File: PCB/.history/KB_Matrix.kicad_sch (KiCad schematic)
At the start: 42 parts

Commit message: Started trying to route the traces
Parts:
- S1, S10, S11, S12, S13, S14, S15, S16, S17, S18, S19, S2, S20, S21, S3, S4, S5, S6, S7, S8, S9: footprint (none) -> Keyboard switches:Kailh_socket_PG1350
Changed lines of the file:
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@@
 			)
 		)
-		(property "Footprint" ""
+		(property "Footprint" "Keyboard switches:Kailh_socket_PG1350"
 			(at 116.84 92.71 0)
 			(hide yes)
@@
 			)
 		)
-		(property "Footprint" ""
+		(property "Footprint" "Keyboard switches:Kailh_socket_PG1350"
 			(at 137.16 106.68 0)
 			(hide yes)
@@
 			)
 		)
-		(property "Footprint" ""
+		(property "Footprint" "Keyboard switches:Kailh_socket_PG1350"
 			(at 137.16 92.71 0)
 			(hide yes)
@@
 			)
 		)
-		(property "Footprint" ""
+		(property "Footprint" "Keyboard switches:Kailh_socket_PG1350"
 			(at 137.16 64.77 0)
 			(hide yes)
@@
 			)
 		)
-		(property "Footprint" ""
+		(property "Footprint" "Keyboard switches:Kailh_socket_PG1350"
 			(at 116.84 64.77 0)
 			(hide yes)
@@
 			)
 		)
-		(property "Footprint" ""
+		(property "Footprint" "Keyboard switches:Kailh_socket_PG1350"
 			(at 147.32 78.74 0)
 			(hide yes)
@@
 			)
 		)
-		(property "Footprint" ""
+		(property "Footprint" "Keyboard switches:Kailh_socket_PG1350"
 			(at 127 92.71 0)
 			(hide yes)
@@
 			)
 		)
-		(property "Footprint" ""
+		(property "Footprint" "Keyboard switches:Kailh_socket_PG1350"
 			(at 106.68 92.71 0)
 			(hide yes)
@@
 			)
 		)
-		(property "Footprint" ""
+		(property "Footprint" "Keyboard switches:Kailh_socket_PG1350"
 			(at 127 120.65 0)
 			(hide yes)
@@
 			)
 		)
-		(property "Footprint" ""
+		(property "Footprint" "Keyboard switches:Kailh_socket_PG1350"
 			(at 116.84 78.74 0)
 			(hide yes)
@@
 			)
 		)
-		(property "Footprint" ""
+		(property "Footprint" "Keyboard switches:Kailh_socket_PG1350"
 			(at 127 64.77 0)
 			(hide yes)
@@
 			)
 		)
-		(property "Footprint" ""
+		(property "Footprint" "Keyboard switches:Kailh_socket_PG1350"
 			(at 106.68 64.77 0)
 			(hide yes)
@@
 			)
 		)
-		(property "Footprint" ""
+		(property "Footprint" "Keyboard switches:Kailh_socket_PG1350"
 			(at 106.68 120.65 0)
 			(hide yes)
@@
 			)
 		)
-		(property "Footprint" ""
+		(property "Footprint" "Keyboard switches:Kailh_socket_PG1350"
 			(at 106.68 78.74 0)
 			(hide yes)
@@
 			)
 		)
-		(property "Footprint" ""
+		(property "Footprint" "Keyboard switches:Kailh_socket_PG1350"
 			(at 106.68 106.68 0)
 			(hide yes)
@@
 			)
 		)
-		(property "Footprint" ""
+		(property "Footprint" "Keyboard switches:Kailh_socket_PG1350"
 			(at 116.84 106.68 0)
 			(hide yes)
@@
 			)
 		)
-		(property "Footprint" ""
+		(property "Footprint" "Keyboard switches:Kailh_socket_PG1350"
 			(at 137.16 78.74 0)
 			(hide yes)
@@
 			)
 		)
-		(property "Footprint" ""
+		(property "Footprint" "Keyboard switches:Kailh_socket_PG1350"
 			(at 147.32 64.77 0)
 			(hide yes)
@@
 			)
 		)
-		(property "Footprint" ""
+		(property "Footprint" "Keyboard switches:Kailh_socket_PG1350"
 			(at 116.84 120.65 0)
 			(hide yes)
@@
 			)
 		)
-		(property "Footprint" ""
+		(property "Footprint" "Keyboard switches:Kailh_socket_PG1350"
 			(at 127 106.68 0)
 			(hide yes)
@@
 			)
 		)
-		(property "Footprint" ""
+		(property "Footprint" "Keyboard switches:Kailh_socket_PG1350"
 			(at 127 78.74 0)
 			(hide yes)

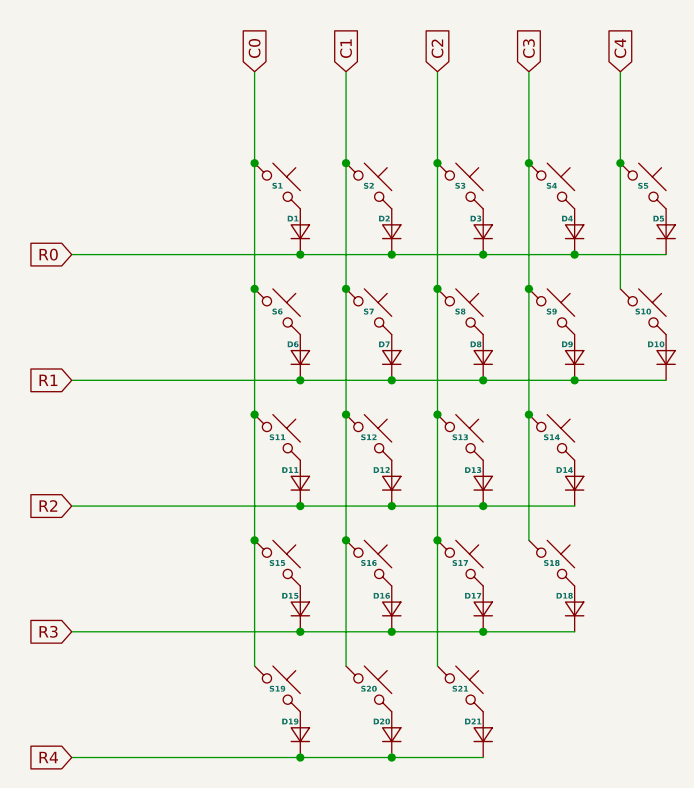
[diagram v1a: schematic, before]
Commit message: Done with the kiCad Matrix layout placement in sketch
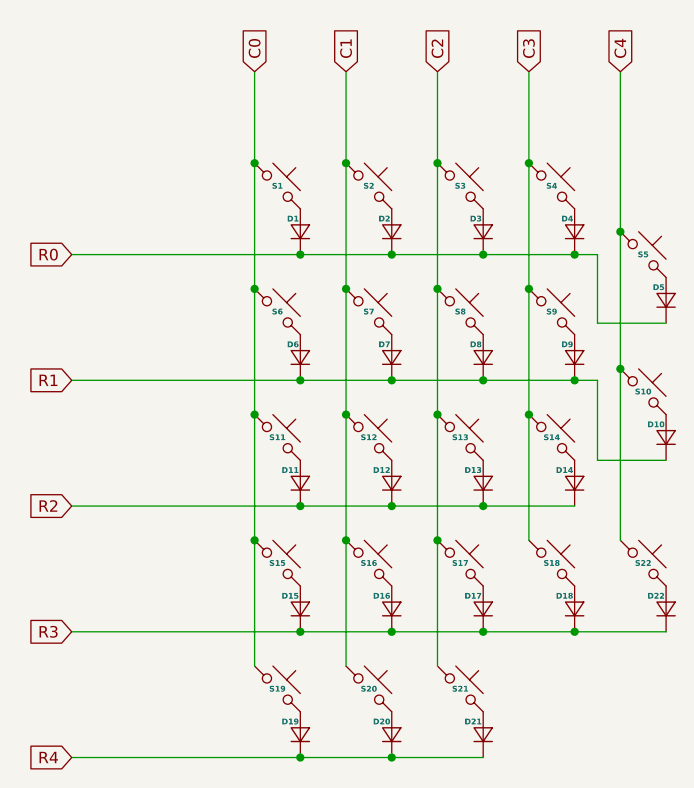
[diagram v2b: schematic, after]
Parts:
- added D22: (no value), Diode_SMD:D_SOD-123, symbol ScottoKeebs:Placeholder_Diode
- added S22: (no value), Keyboard switches:Kailh_socket_PG1350, symbol ScottoKeebs:Placeholder_Keyswitch
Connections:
- net C4: now also S22.1
- net R3: now also D22.1 (K)
- new net: D22.2 (A), S22.2
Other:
- moved on the sheet: D10, S10

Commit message: Improved routing and the first final iteration of PCB
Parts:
- added D23: (no value), Diode_SMD:D_SOD-123, symbol ScottoKeebs:Placeholder_Diode
- added S23: (no value), ScottoKeebs_Choc:Hotswap_Choc_V1_1.00u, symbol ScottoKeebs:Placeholder_Keyswitch
- S1, S10, S11, S12, S13, S14, S15, S16, S17, S18, S19, S2, S20, S21, S22, S3, S4, S5, S6, S7, S8, S9: footprint Keyboard switches:Kailh_socket_PG1350 -> ScottoKeebs_Choc:Hotswap_Choc_V1_1.00u
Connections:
- net C4: now also S23.1
- net R4: now also D23.1 (K)
- new net: D23.2 (A), S23.2
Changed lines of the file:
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@@
 	)
 	(junction
+		(at 144.78 104.14)
+		(diameter 0)
+		(color 0 0 0 0)
+	)
+	(junction
 		(at 114.3 62.23)
 		(diameter 0)
@@
 	)
 	(junction
+		(at 129.54 128.27)
+		(diameter 0)
+		(color 0 0 0 0)
+	)
+	(junction
 		(at 109.22 100.33)
 		(diameter 0)
@@
 	(wire
 		(pts
+			(xy 144.78 104.14) (xy 144.78 118.11)
+		)
+		(stroke
+			(width 0)
+			(type default)
+		)
+	)
+	(wire
+		(pts
 			(xy 114.3 90.17) (xy 114.3 104.14)
 		)
@@
 	(wire
 		(pts
+			(xy 129.54 128.27) (xy 149.86 128.27)
+		)
+		(stroke
+			(width 0)
+			(type default)
+		)
+	)
+	(wire
+		(pts
 			(xy 109.22 114.3) (xy 119.38 114.3)
 		)
@@
 			)
 		)
-		(property "Footprint" "Keyboard switches:Kailh_socket_PG1350"
+		(property "Footprint" "ScottoKeebs_Choc:Hotswap_Choc_V1_1.00u"
 			(at 116.84 92.71 0)
 			(hide yes)
@@
 			)
 		)
-		(property "Footprint" "Keyboard switches:Kailh_socket_PG1350"
+		(property "Footprint" "ScottoKeebs_Choc:Hotswap_Choc_V1_1.00u"
 			(at 137.16 106.68 0)
 			(hide yes)
@@
 			)
 		)
-		(property "Footprint" "Keyboard switches:Kailh_socket_PG1350"
+		(property "Footprint" "ScottoKeebs_Choc:Hotswap_Choc_V1_1.00u"
 			(at 147.32 106.68 0)
 			(hide yes)
@@
 			)
 		)
-		(property "Footprint" "Keyboard switches:Kailh_socket_PG1350"
+		(property "Footprint" "ScottoKeebs_Choc:Hotswap_Choc_V1_1.00u"
 			(at 147.32 72.39 0)
 			(hide yes)
@@
 			)
 		)
-		(property "Footprint" "Keyboard switches:Kailh_socket_PG1350"
+		(property "Footprint" "ScottoKeebs_Choc:Hotswap_Choc_V1_1.00u"
 			(at 137.16 92.71 0)
 			(hide yes)
@@
 			)
 		)
-		(property "Footprint" "Keyboard switches:Kailh_socket_PG1350"
+		(property "Footprint" "ScottoKeebs_Choc:Hotswap_Choc_V1_1.00u"
 			(at 137.16 64.77 0)
 			(hide yes)
@@
 			)
 		)
-		(property "Footprint" "Keyboard switches:Kailh_socket_PG1350"
+		(property "Footprint" "ScottoKeebs_Choc:Hotswap_Choc_V1_1.00u"
 			(at 116.84 64.77 0)
 			(hide yes)
@@
 			)
 		)
-		(property "Footprint" "Keyboard switches:Kailh_socket_PG1350"
+		(property "Footprint" "ScottoKeebs_Choc:Hotswap_Choc_V1_1.00u"
 			(at 147.32 87.63 0)
 			(hide yes)
@@
 			)
 		)
-		(property "Footprint" "Keyboard switches:Kailh_socket_PG1350"
+		(property "Footprint" "ScottoKeebs_Choc:Hotswap_Choc_V1_1.00u"
 			(at 127 92.71 0)
 			(hide yes)
@@
 			)
 		)
-		(property "Footprint" "Keyboard switches:Kailh_socket_PG1350"
+		(property "Footprint" "ScottoKeebs_Choc:Hotswap_Choc_V1_1.00u"
 			(at 106.68 92.71 0)
 			(hide yes)
@@
 	)
 	(symbol
+		(lib_id "ScottoKeebs:Placeholder_Keyswitch")
+		(at 147.32 120.65 0)
+		(unit 1)
+		(body_style 1)
+		(exclude_from_sim no)
+		(in_bom yes)
+		(on_board yes)
+		(in_pos_files yes)
+		(dnp no)
+		(fields_autoplaced yes)
+		(property "Reference" "S23"
+			(at 147.32 120.65 0)
+			(show_name no)
+			(do_not_autoplace yes)
+			(effects
+				(font
+					(size 0.635 0.635)
+					(thickness 0.127)
+					(bold yes)
+				)
+			)
+		)
+		(property "Value" ""
+			(at 147.32 124.46 0)
+			(show_name no)
+			(do_not_autoplace no)
+			(effects
+				(font
+					(size 1.27 1.27)
+				)
+			)
+		)
+		(property "Footprint" "ScottoKeebs_Choc:Hotswap_Choc_V1_1.00u"
+			(at 147.32 120.65 0)
+			(hide yes)
+			(show_name no)
+			(do_not_autoplace no)
+			(effects
+				(font
+					(size 1.27 1.27)
+				)
+			)
+		)
+		(property "Datasheet" ""
+			(at 144.78 122.428 0)
+			(hide yes)
+			(show_name no)
+			(do_not_autoplace no)
+			(effects
+				(font
+					(size 1.27 1.27)
+				)
+			)
+		)
+		(property "Description" ""
+			(at 147.32 120.65 0)
+			(hide yes)
+			(show_name no)
+			(do_not_autoplace no)
+			(effects
+				(font
+					(size 1.27 1.27)
+				)
+			)
+		)
+		(pin "1"
+		)
+		(pin "2"
+		)
+		(instances
+			(project "PCB"
+				(path "/61897acb-2078-4c47-92ce-82a0439bac7e/a92edfaf-c5c9-4d6d-a061-75eff395646f"
+					(reference "S23")
+					(unit 1)
+				)
+			)
+		)
+	)
+	(symbol
 		(lib_id "ScottoKeebs:Placeholder_Diode")
 		(at 129.54 125.73 0)
@@
 			)
 		)
-		(property "Footprint" "Keyboard switches:Kailh_socket_PG1350"
+		(property "Footprint" "ScottoKeebs_Choc:Hotswap_Choc_V1_1.00u"
 			(at 127 120.65 0)
 			(hide yes)
@@
 			)
 		)
-		(property "Footprint" "Keyboard switches:Kailh_socket_PG1350"
+		(property "Footprint" "ScottoKeebs_Choc:Hotswap_Choc_V1_1.00u"
 			(at 116.84 78.74 0)
 			(hide yes)
@@
 			)
 		)
-		(property "Footprint" "Keyboard switches:Kailh_socket_PG1350"
+		(property "Footprint" "ScottoKeebs_Choc:Hotswap_Choc_V1_1.00u"
 			(at 127 64.77 0)
 			(hide yes)
@@
 			)
 		)
-		(property "Footprint" "Keyboard switches:Kailh_socket_PG1350"
+		(property "Footprint" "ScottoKeebs_Choc:Hotswap_Choc_V1_1.00u"
 			(at 106.68 64.77 0)
 			(hide yes)
@@
 			)
 		)
-		(property "Footprint" "Keyboard switches:Kailh_socket_PG1350"
+		(property "Footprint" "ScottoKeebs_Choc:Hotswap_Choc_V1_1.00u"
 			(at 106.68 120.65 0)
 			(hide yes)
@@
 			)
 		)
-		(property "Footprint" "Keyboard switches:Kailh_socket_PG1350"
+		(property "Footprint" "ScottoKeebs_Choc:Hotswap_Choc_V1_1.00u"
 			(at 106.68 78.74 0)
 			(hide yes)
@@
 			)
 		)
-		(property "Footprint" "Keyboard switches:Kailh_socket_PG1350"
+		(property "Footprint" "ScottoKeebs_Choc:Hotswap_Choc_V1_1.00u"
 			(at 106.68 106.68 0)
 			(hide yes)
@@
 			)
 		)
-		(property "Footprint" "Keyboard switches:Kailh_socket_PG1350"
+		(property "Footprint" "ScottoKeebs_Choc:Hotswap_Choc_V1_1.00u"
 			(at 116.84 106.68 0)
 			(hide yes)
@@
 			)
 		)
-		(property "Footprint" "Keyboard switches:Kailh_socket_PG1350"
+		(property "Footprint" "ScottoKeebs_Choc:Hotswap_Choc_V1_1.00u"
 			(at 137.16 78.74 0)
 			(hide yes)
@@
 			)
 		)
-		(property "Footprint" "Keyboard switches:Kailh_socket_PG1350"
+		(property "Footprint" "ScottoKeebs_Choc:Hotswap_Choc_V1_1.00u"
 			(at 116.84 120.65 0)
 			(hide yes)
@@
 	)
 	(symbol
+		(lib_id "ScottoKeebs:Placeholder_Diode")
+		(at 149.86 125.73 0)
+		(unit 1)
+		(body_style 1)
+		(exclude_from_sim no)
+		(in_bom yes)
+		(on_board yes)
+		(in_pos_files yes)
+		(dnp no)
+		(fields_autoplaced yes)
+		(property "Reference" "D23"
+			(at 149.71 124.664 0)
+			(show_name no)
+			(do_not_autoplace yes)
+			(effects
+				(font
+					(size 0.635 0.635)
+					(thickness 0.127)
+					(bold yes)
+				)
+				(justify right bottom)
+			)
+		)
+		(property "Value" ""
+			(at 152.4 125.73 90)
+			(show_name no)
+			(do_not_autoplace no)
+			(effects
+				(font
+					(size 1.27 1.27)
+				)
+			)
+		)
+		(property "Footprint" "Diode_SMD:D_SOD-123"
+			(at 149.86 125.73 90)
+			(hide yes)
+			(show_name no)
+			(do_not_autoplace no)
+			(effects
+				(font
+					(size 1.27 1.27)
+				)
+			)
+		)
+		(property "Datasheet" ""
+			(at 149.86 125.73 90)
+			(hide yes)
+			(show_name no)
+			(do_not_autoplace no)
+			(effects
+				(font
+					(size 1.27 1.27)
+				)
+			)
+		)
+		(property "Description" ""
+			(at 153.67 125.73 90)
+			(hide yes)
+			(show_name no)
+			(do_not_autoplace no)
+			(effects
+				(font
+					(size 1.27 1.27)
+				)
+			)
+		)
+		(pin "2"
+		)
+		(pin "1"
+		)
+		(instances
+			(project "PCB"
+				(path "/61897acb-2078-4c47-92ce-82a0439bac7e/a92edfaf-c5c9-4d6d-a061-75eff395646f"
+					(reference "D23")
+					(unit 1)
+				)
+			)
+		)
+	)
+	(symbol
 		(lib_id "ScottoKeebs:Placeholder_Keyswitch")
 		(at 127 106.68 0)
@@
 			)
 		)
-		(property "Footprint" "Keyboard switches:Kailh_socket_PG1350"
+		(property "Footprint" "ScottoKeebs_Choc:Hotswap_Choc_V1_1.00u"
 			(at 127 106.68 0)
 			(hide yes)
@@
 			)
 		)
-		(property "Footprint" "Keyboard switches:Kailh_socket_PG1350"
+		(property "Footprint" "ScottoKeebs_Choc:Hotswap_Choc_V1_1.00u"
 			(at 127 78.74 0)
 			(hide yes)
